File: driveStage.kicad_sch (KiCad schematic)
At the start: 64 parts, among them J1 MOD_IN, K1 DIP12-1C90-51L, Q1 SQJA70EP-T1, Q7 BSS138, SW1 SW_DIP_x03, U1 LTC6655BHLS8-4.096, U2 MAX5719xSD, U3 ADA4898-1YRDZ, U4 ADA4898-1YRDZ, U5 LM358, U6 ADA4898-1YRDZ

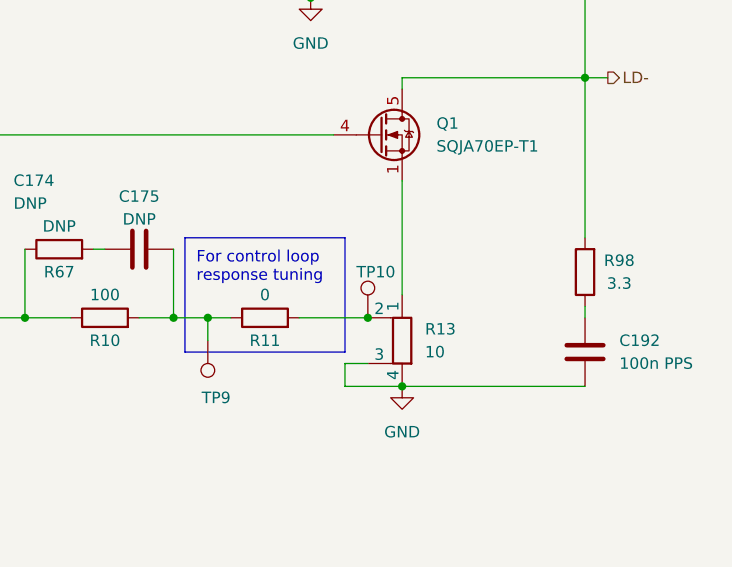
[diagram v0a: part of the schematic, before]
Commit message: sch: R13 Power Resistor change to PDY10R000F
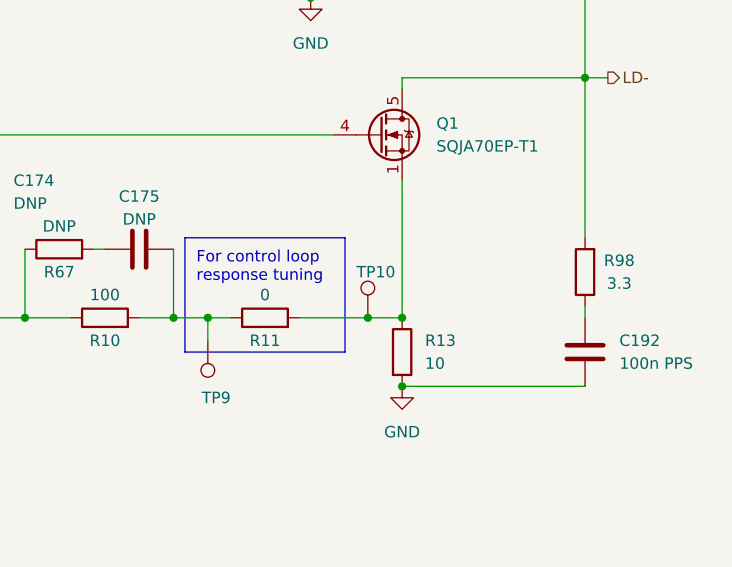
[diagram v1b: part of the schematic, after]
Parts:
- removed R13: 10, kirdy:R_Shunt_VCS1625ZP, symbol Device:R_Shunt
- added R13: 10, Package_TO_SOT_THT:TO-220-2_Horizontal_TabDown, symbol Device:R
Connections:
- net GND: now also R13.2
- net at R11.2, TP10.1: now also Q1.1 (S), Q1.2 (S), Q1.3 (S), R13.1

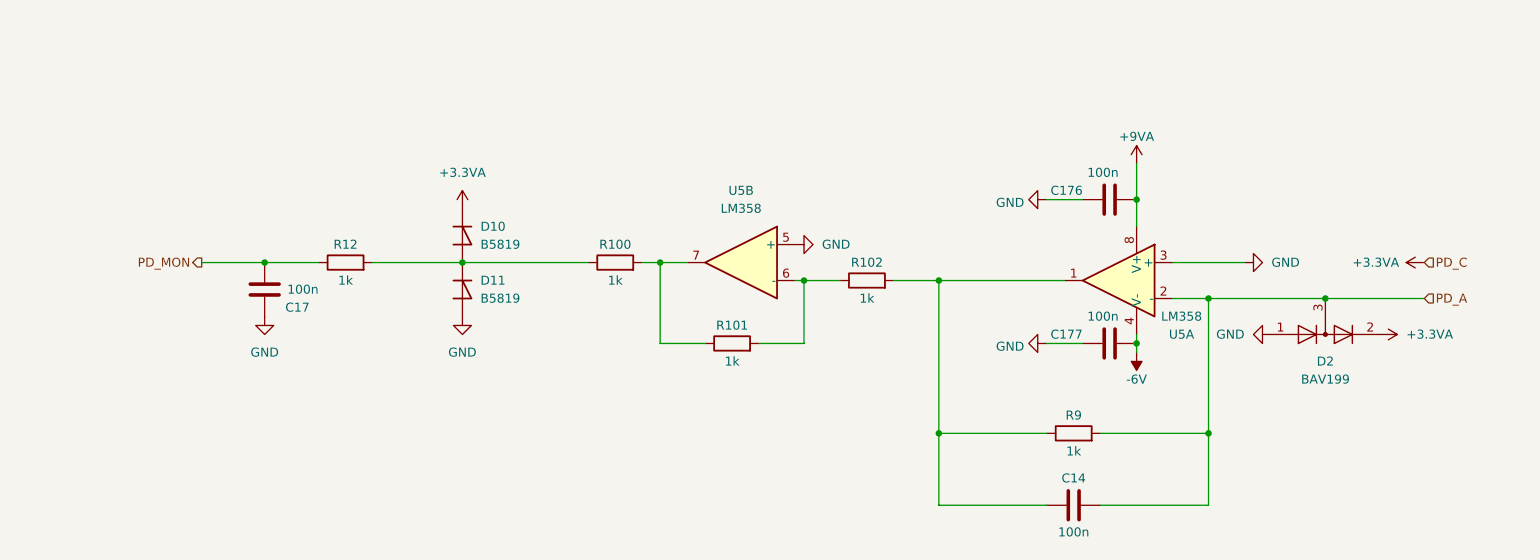
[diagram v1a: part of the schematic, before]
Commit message: sch: Use TL082 for PD_Mon TIA and LPF Stage
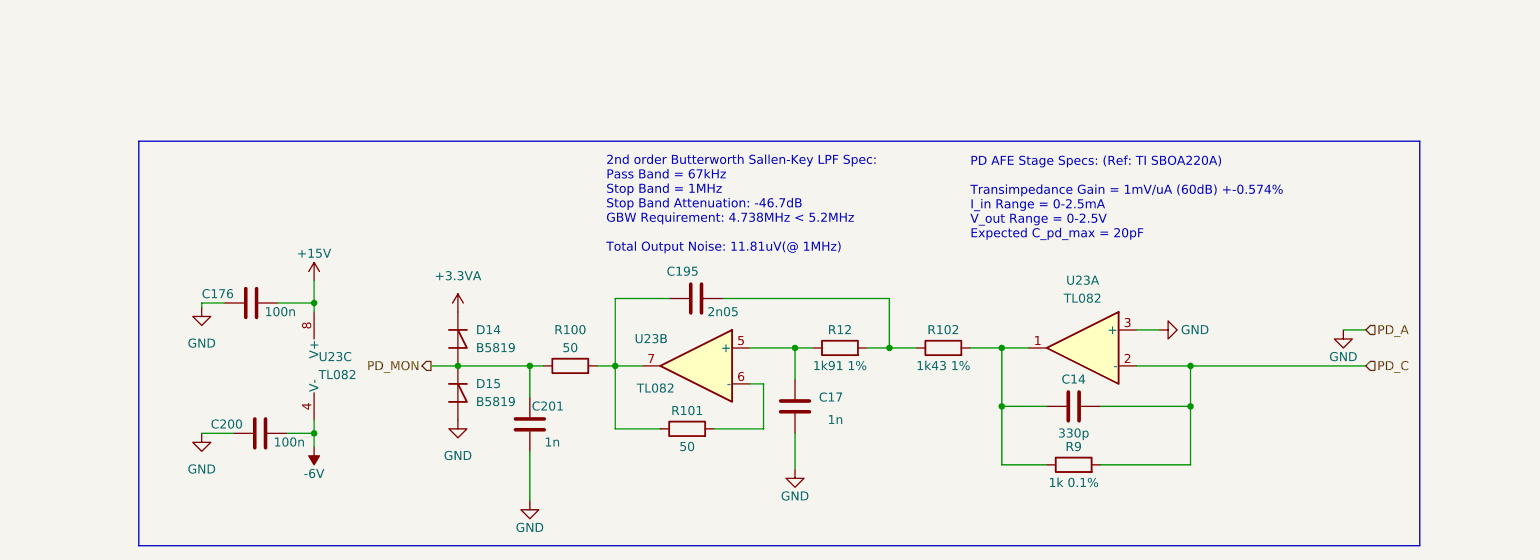
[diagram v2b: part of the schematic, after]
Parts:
- removed C177: 100n, Capacitor_SMD:C_0603_1608Metric, symbol Device:C
- removed D10, D11: B5819, Diode_SMD:D_SOD-323, symbol Device:D_Shockley
- removed D2: BAV199, Package_TO_SOT_SMD:SOT-23, symbol Diode:BAV99
- removed U5: LM358, Package_SO:SOIC-8_3.9x4.9mm_P1.27mm, symbol Amplifier_Operational:LM358
- added C195: 2n05, Capacitor_SMD:C_0603_1608Metric, symbol Device:C
- added C200: 100n, Capacitor_SMD:C_0603_1608Metric, symbol Device:C
- added C201: 1n, Capacitor_SMD:C_0603_1608Metric, symbol Device:C
- added D14, D15: B5819, Diode_SMD:D_SOD-323, symbol Device:D_Shockley
- added U23: TL082, symbol Amplifier_Operational:TL082
- C14: value 100n -> 330p; MFR_PN GCM1885C1H162FA16D -> (none); MFR_PN_ALT C0603C162J5GAC7867 -> (none)
- C17: value 100n -> 1n; MFR_PN CL10B104KB8NNWC -> (none); MFR_PN_ALT CL10B104KB8NNNL -> (none)
- R100: value 1k -> 50; MFR_PN RNCP0603FTD1K00 -> (none); MFR_PN_ALT WR06X1001FTL -> RC0603FR-10300RL
- R101: value 1k -> 50; MFR_PN RNCP0603FTD1K00 -> (none)
- R102: value 1k -> 1k43 1%; MFR_PN RNCP0603FTD1K00 -> (none)
- R12: value 1k -> 1k91 1%; MFR_PN RNCP0603FTD1K00 -> (none)
- R9: value 1k -> 1k 0.1%; MFR_PN RNCP0603FTD1K00 -> RP0603BRD071KL
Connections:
- net +15V: now also C176.1, U23.8 (V+)
- net +3.3VA: now also D14.1 (K)
- net +9VA: no longer C176.2
- net -6V: now also C200.1, U23.4 (V-)
- net GND: now also C176.2, C200.2, C201.1, D15.2 (A), U23.3 (+); no longer C176.1
- net PD_MON: now also R100.1, C201.2, D14.2 (A), D15.1 (K); no longer C17.2, R12.1
- net at R100.2, R101.1: now also C195.2, U23.7
- net at R102.1: now also R12.2, C195.1; no longer R101.2
- net at C14.1, R102.2, R9.1: now also U23.1
- net PD_A renamed PD_C
- net PD_C: now also U23.2 (-)
- new net: C17.2, R12.1, U23.5 (+)
- new net: R101.2, U23.6 (-)
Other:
- note added: "2nd order Butterworth Sallen-Key LPF Spec: Pass Band = 67kHz Stop Band = 1MHz Stop Band Attenuation: -46.7dB GBW Requirement: 4.738MHz < 5.2MHz Total Output Noise: 11.81uV(@ 1MHz)"
- note added: "PD AFE Stage Specs: (Ref: TI SBOA220A) Transimpedance Gain = 1mV/uA (60dB) +-0.574% I_in Range = 0-2.5mA V_out Range = 0-2.5V Expected C_pd_max = 20pF"

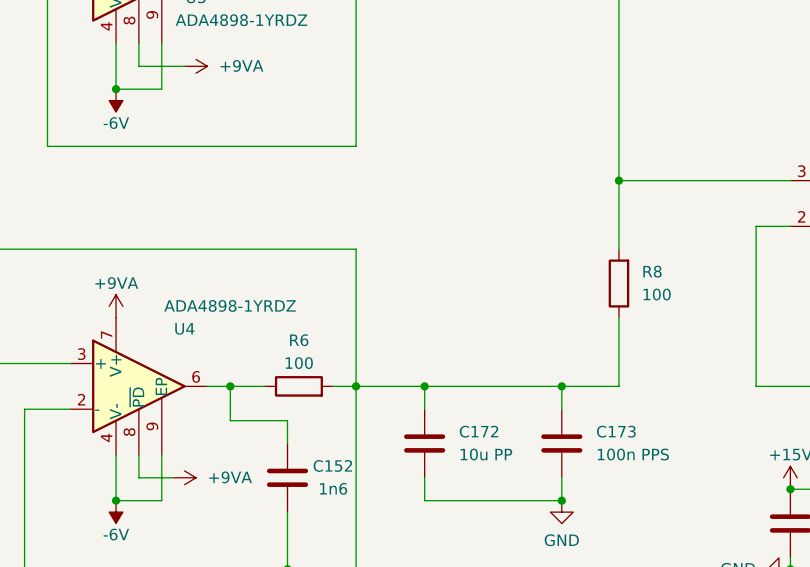
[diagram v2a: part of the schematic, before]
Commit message: sch: LD DAC add parallel Cap to output resistor - Increase the Mod_In Signal Bandwidth - See Issue #22
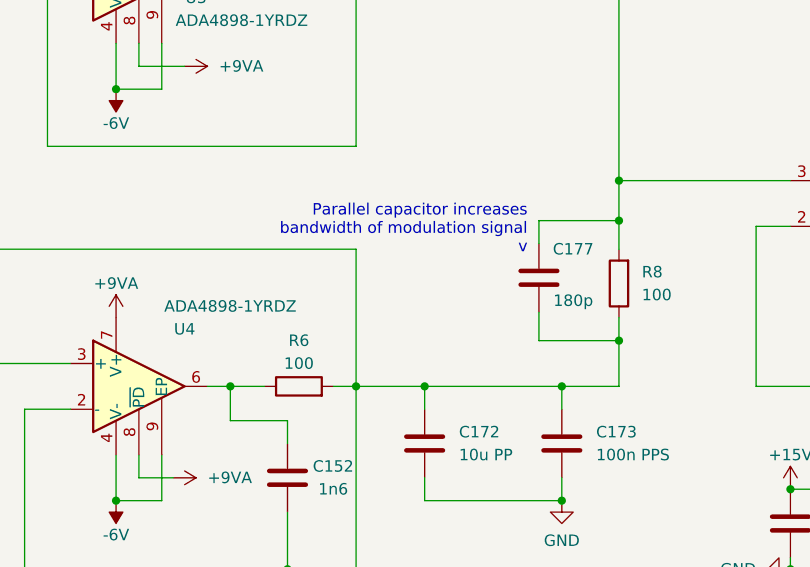
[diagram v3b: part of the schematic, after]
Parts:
- added C177: 180p, Capacitor_SMD:C_0603_1608Metric, symbol Device:C
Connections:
- net at C152.1, C172.1, C173.1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: now also C177.2
- net at R7.2, R8.2, U6.3 (+): now also C177.1
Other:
- note added: "Parallel capacitor increases bandwidth of modulation signal v"
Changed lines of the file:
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@@
   (junction (at 210.185 219.71) (diameter 0) (color 0 0 0 0)
   )
+  (junction (at 246.38 110.49) (diameter 0) (color 0 0 0 0)
+  )
   (junction (at 246.38 92.71) (diameter 0) (color 0 0 0 0)
   )
@@
   )
   (junction (at 336.55 59.69) (diameter 0) (color 0 0 0 0)
+  )
+  (junction (at 246.38 97.155) (diameter 0) (color 0 0 0 0)
   )
   (junction (at 344.17 39.37) (diameter 0) (color 0 0 0 0)
@@
     (stroke (width 0) (type default))
   )
+  (wire (pts (xy 237.49 107.315) (xy 237.49 110.49))
+    (stroke (width 0) (type default))
+  )
   (wire (pts (xy 318.77 59.69) (xy 336.55 59.69))
     (stroke (width 0) (type default))
@@
     (stroke (width 0) (type default))
   )
+  (wire (pts (xy 246.38 107.95) (xy 246.38 110.49))
+    (stroke (width 0) (type default))
+  )
   (wire (pts (xy 367.03 114.3) (xy 367.03 115.57))
     (stroke (width 0) (type default))
@@
     (stroke (width 0) (type default))
   )
+  (wire (pts (xy 237.49 110.49) (xy 246.38 110.49))
+    (stroke (width 0) (type default))
+  )
   (wire (pts (xy 252.73 200.66) (xy 252.73 210.185))
     (stroke (width 0) (type default))
@@
     (stroke (width 0) (type default))
   )
+  (wire (pts (xy 237.49 97.155) (xy 246.38 97.155))
+    (stroke (width 0) (type default))
+  )
   (polyline (pts (xy 322.58 106.68) (xy 340.36 106.68))
     (stroke (width 0) (type default))
@@
     (stroke (width 0) (type default))
   )
-  (wire (pts (xy 246.38 92.71) (xy 246.38 100.33))
+  (wire (pts (xy 246.38 97.155) (xy 246.38 100.33))
     (stroke (width 0) (type default))
   )
@@
     (stroke (width 0) (type default))
   )
+  (wire (pts (xy 246.38 92.71) (xy 246.38 97.155))
+    (stroke (width 0) (type default))
+  )
   (polyline (pts (xy 29.21 135.89) (xy 176.53 135.89))
     (stroke (width 0) (type default))
@@
     (stroke (width 0) (type default))
   )
-  (wire (pts (xy 246.38 107.95) (xy 246.38 115.57))
+  (wire (pts (xy 246.38 110.49) (xy 246.38 115.57))
     (stroke (width 0) (type default))
   )
@@
   )
   (polyline (pts (xy 176.53 135.89) (xy 176.53 87.63))
+    (stroke (width 0) (type default))
+  )
+  (wire (pts (xy 237.49 99.695) (xy 237.49 97.155))
     (stroke (width 0) (type default))
   )
@@
     (at 251.46 194.31 0)
     (effects (font (size 1.27 1.27)) (justify left bottom))
+  )
+  (text "Parallel capacitor increases \nbandwidth of modulation signal\nv"
+    (at 236.22 100.965 0)
+    (effects (font (size 1.27 1.27)) (justify right bottom))
   )
   (text "Modulation Depth" (at 160.02 55.88 0)
@@
         )
       )
+    )
+  )
+  (symbol (lib_id "Device:C") (at 237.49 103.505 0) (unit 1)
+    (in_bom yes) (on_board yes) (dnp no)
+    (property "Reference" "C177" (at 241.3 100.33 0)
+      (effects (font (size 1.27 1.27)))
+    )
+    (property "Value" "180p" (at 241.3 106.045 0)
+      (effects (font (size 1.27 1.27)))
+    )
+    (property "Footprint" "Capacitor_SMD:C_0603_1608Metric" (at 238.4552 107.315 0)
+      (effects (font (size 1.27 1.27)) hide)
+    )
+    (property "Datasheet" "~" (at 237.49 103.505 0)
+      (effects (font (size 1.27 1.27)) hide)
+    )
+    (property "MFR_PN" "" (at 237.49 103.505 0)
+      (effects (font (size 1.27 1.27)) hide)
+    )
+    (property "MFR_PN_ALT" "CL10B104KB8NNNL" (at 237.49 103.505 0)
+      (effects (font (size 1.27 1.27)) hide)
+    )
+    (pin "1")
+    (pin "2")
+    (instances
+      (project "kirdy"
+        (path "/88da1dd8-9274-4b55-84fb-90006c9b6e8f/7fc2620b-bac4-49c0-a276-7d2a46898037"
+          (reference "C177") (unit 1)
+        )
+      )

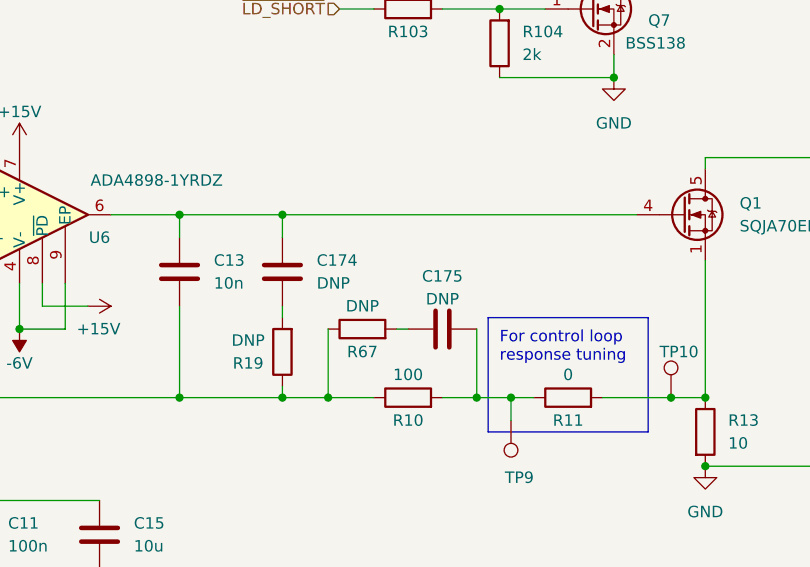
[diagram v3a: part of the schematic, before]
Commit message: sch: Tune the LD V-I Output Stage Feedback Network - R67 -> 0R - C175 -> 100pF
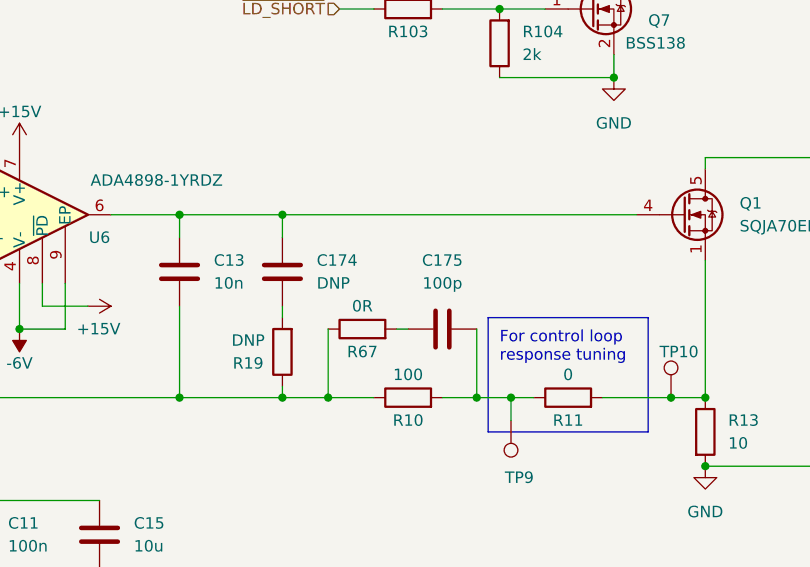
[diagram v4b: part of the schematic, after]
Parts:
- C175: value DNP -> 100p
- R67: value DNP -> 0R
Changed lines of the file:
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@@
   (symbol (lib_id "Device:C") (at 317.5 107.95 90) (unit 1)
     (in_bom yes) (on_board yes) (dnp no) (fields_autoplaced)
-    (property "Reference" "C175" (at 317.5 102.0912 90)
+    (property "Reference" "C175" (at 317.5 100.33 90)
       (effects (font (size 1.27 1.27)))
     )
-    (property "Value" "DNP" (at 317.5 104.6281 90)
+    (property "Value" "100p" (at 317.5 102.87 90)
       (effects (font (size 1.27 1.27)))
     )
@@
       (effects (font (size 1.27 1.27)))
     )
-    (property "Value" "DNP" (at 308.61 105.41 90)
+    (property "Value" "0R" (at 308.61 105.41 90)
       (effects (font (size 1.27 1.27)))
     )

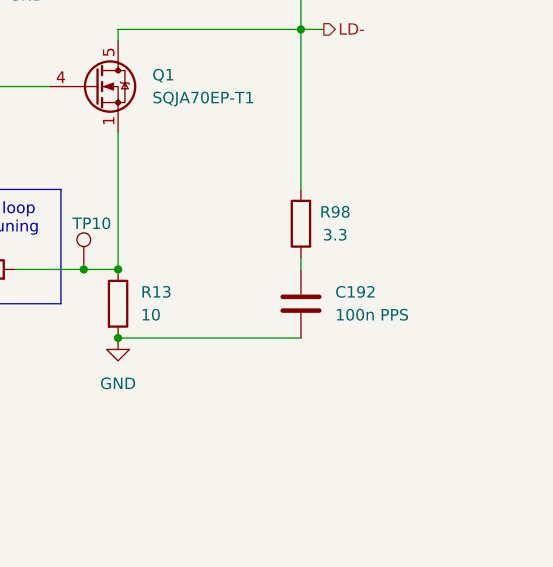
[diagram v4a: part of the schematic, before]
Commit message: sch: Tune LD- Out Series RC Network - R98 3R3 -> 10R - C192 100n PPS -> DNP - Add C199 2n2 in parallel C192
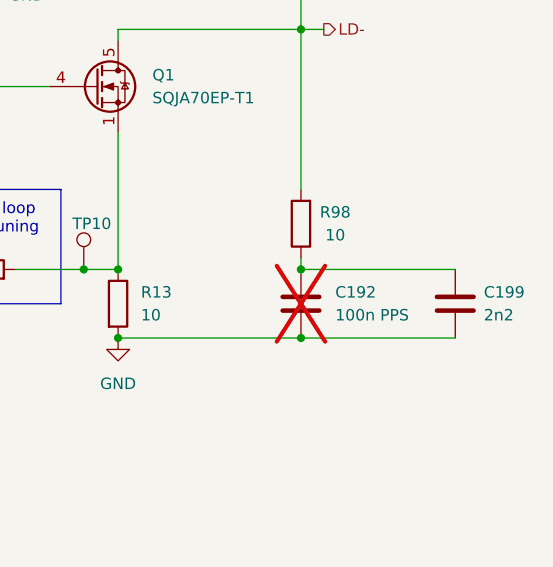
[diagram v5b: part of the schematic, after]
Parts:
- added C199: 2n2, Capacitor_SMD:C_0603_1608Metric, symbol Device:C
- C192: now not fitted
- R98: value 3.3 -> 10
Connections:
- net GND: now also C199.1
- net at C192.1, R98.1: now also C199.2
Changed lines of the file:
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@@
   (junction (at 291.465 207.645) (diameter 0) (color 0 0 0 0)
   )
+  (junction (at 367.03 123.19) (diameter 0) (color 0 0 0 0)
+  )
   (junction (at 93.98 105.41) (diameter 0) (color 0 0 0 0)
   )
@@
   (junction (at 209.55 135.89) (diameter 0) (color 0 0 0 0)
   )
+  (junction (at 367.03 115.57) (diameter 0) (color 0 0 0 0)
+  )
   (junction (at 240.665 210.185) (diameter 0) (color 0 0 0 0)
   )
@@
     (stroke (width 0) (type default))
   )
+  (wire (pts (xy 367.03 115.57) (xy 384.175 115.57))
+    (stroke (width 0) (type default))
+  )
   (wire (pts (xy 252.73 210.185) (xy 252.73 219.075))
     (stroke (width 0) (type default))
@@
     (stroke (width 0) (type default))
   )
+  (wire (pts (xy 367.03 123.19) (xy 384.175 123.19))
+    (stroke (width 0) (type default))
+  )
   (wire (pts (xy 193.04 80.01) (xy 198.12 80.01))
     (stroke (width 0) (type default))
@@
       (effects (font (size 1.27 1.27)))
     )
-    (property "Value" "3.3" (at 370.84 111.76 0)
+    (property "Value" "10" (at 370.84 111.76 0)
       (effects (font (size 1.27 1.27)))
     )
@@
   )
   (symbol (lib_id "Device:C") (at 367.03 119.38 0) (unit 1)
-    (in_bom yes) (on_board yes) (dnp no) (fields_autoplaced)
+    (in_bom yes) (on_board yes) (dnp yes) (fields_autoplaced)
     (property "Reference" "C192" (at 370.84 118.1099 0)
       (effects (font (size 1.27 1.27)) (justify left))
@@
         )
       )
+    )
+  )
+  (symbol (lib_id "Device:C") (at 384.175 119.38 180) (unit 1)
+    (in_bom yes) (on_board yes) (dnp no) (fields_autoplaced)
+    (property "Reference" "C199" (at 387.35 118.11 0)
+      (effects (font (size 1.27 1.27)) (justify right))
+    )
+    (property "Value" "2n2" (at 387.35 120.65 0)
+      (effects (font (size 1.27 1.27)) (justify right))
+    )
+    (property "Footprint" "Capacitor_SMD:C_0603_1608Metric" (at 383.2098 115.57 0)
+      (effects (font (size 1.27 1.27)) hide)
+    )
+    (property "Datasheet" "~" (at 384.175 119.38 0)
+      (effects (font (size 1.27 1.27)) hide)
+    )
+    (property "MFR_PN" "" (at 384.175 119.38 0)
+      (effects (font (size 1.27 1.27)) hide)
+    )
+    (property "MFR_PN_ALT" "" (at 384.175 119.38 0)
+      (effects (font (size 1.27 1.27)) hide)
+    )
+    (pin "1")
+    (pin "2")
+    (instances
+      (project "kirdy"
+        (path "/88da1dd8-9274-4b55-84fb-90006c9b6e8f/7fc2620b-bac4-49c0-a276-7d2a46898037"
+          (reference "C199") (unit 1)
+        )
+      )
